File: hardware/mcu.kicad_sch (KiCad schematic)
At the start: 65 parts, among them J501 TC2050, J502 PRPC006SAAN-RC, J503 PRPC006SAAN-RC, J504 PRPC006SAAN-RC, J505 PRPC006SAAN-RC, J506 PRPC006SAAN-RC, J507 PRPC006SAAN-RC, J508 PRPC006SAAN-RC, J509 PRPC001DAAN-RC, Q501 BSS806NH, U501 STM32L552CEU6, U502 AT25SF081B-MAHB-T, Y501 ECS-160-9-37-CKM-TR3, Y502 ABS05-32.768KHZ-9-T

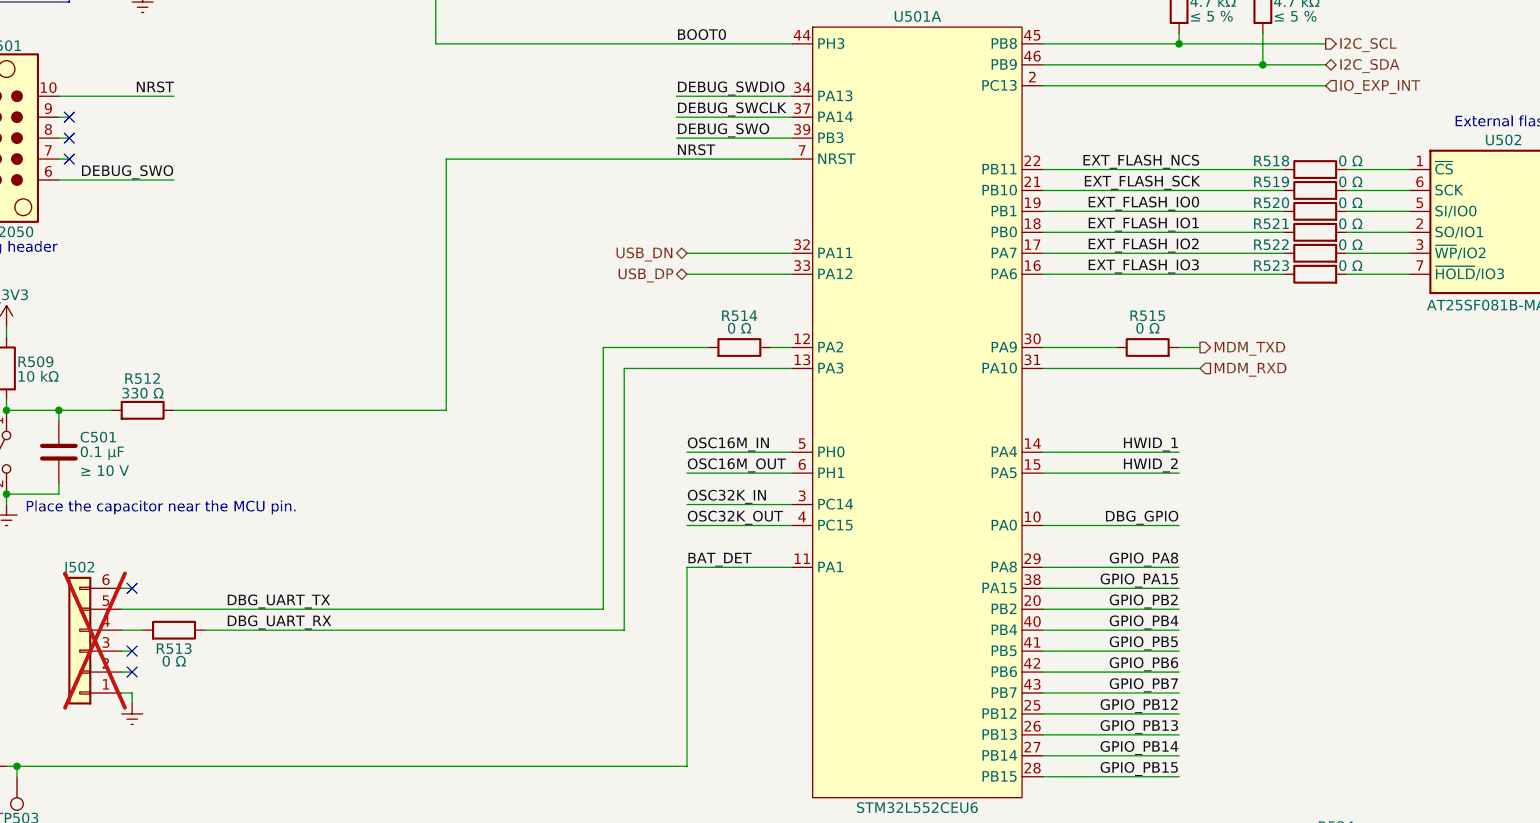
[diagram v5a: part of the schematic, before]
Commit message: HW: Set terminator resistors
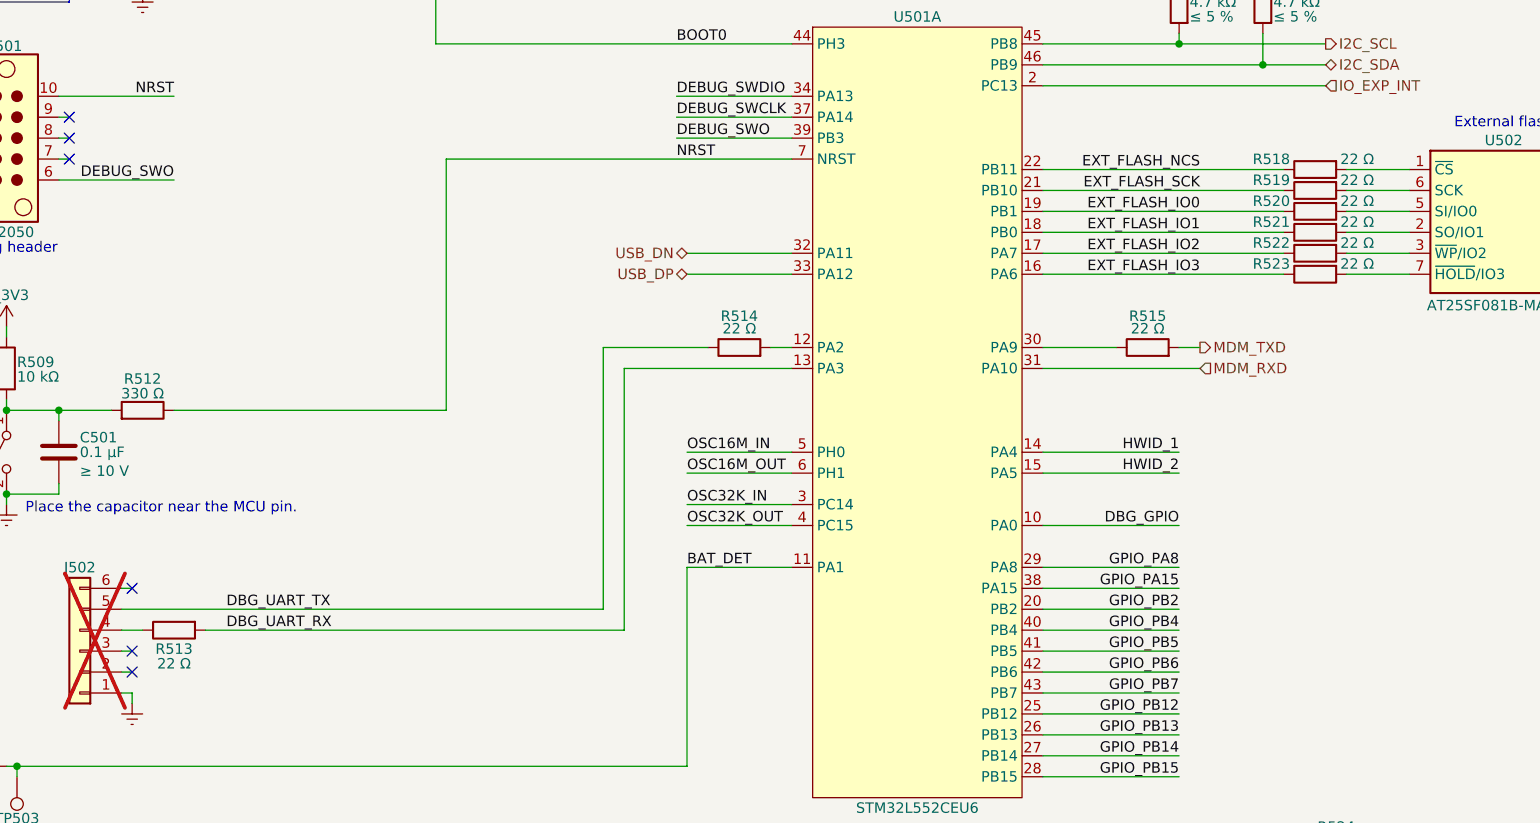
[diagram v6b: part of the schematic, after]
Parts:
- R513, R514, R515, R518, R519, R520, R521, R522, R523: value 0 Ω -> 22 Ω; DigiKey Part Number 732-560112110001CT-ND -> 732-560112110046CT-ND; MPN 560112110001 -> 560112110046
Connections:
- net DBG_UART_RX: now also R513.2; no longer R513.1
- net DBG_UART_TX: now also R514.1; no longer R514.2
- net at J502.4 (Pin_4): now also R513.1; no longer R513.2
- net at U501.12 (PA2): now also R514.2; no longer R514.1

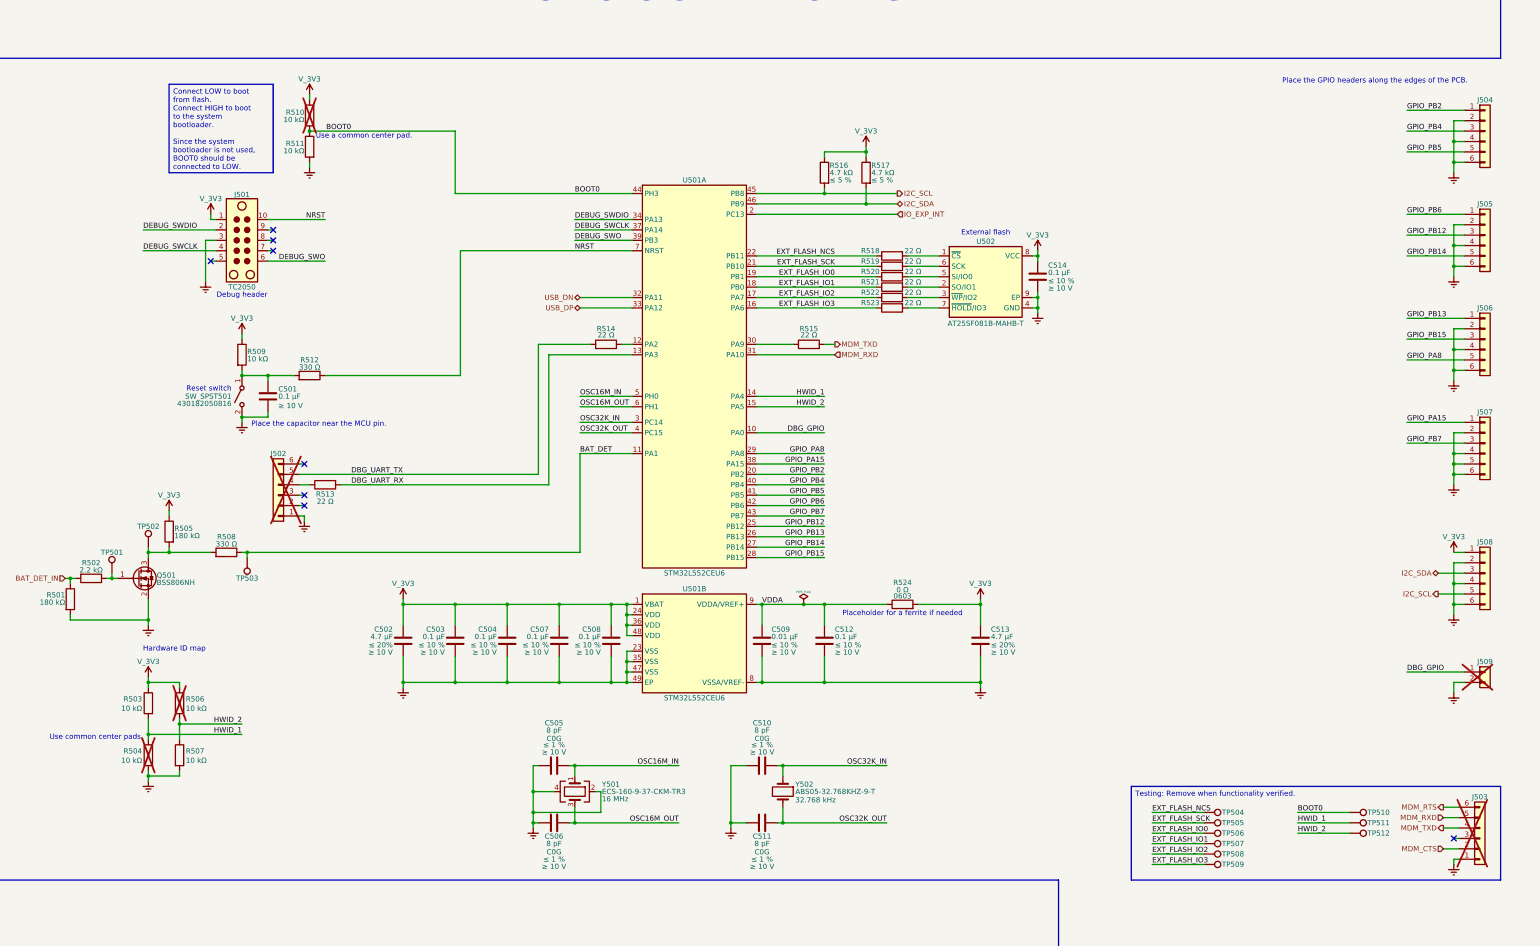
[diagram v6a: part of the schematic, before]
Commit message: HW: Refactor reference designators
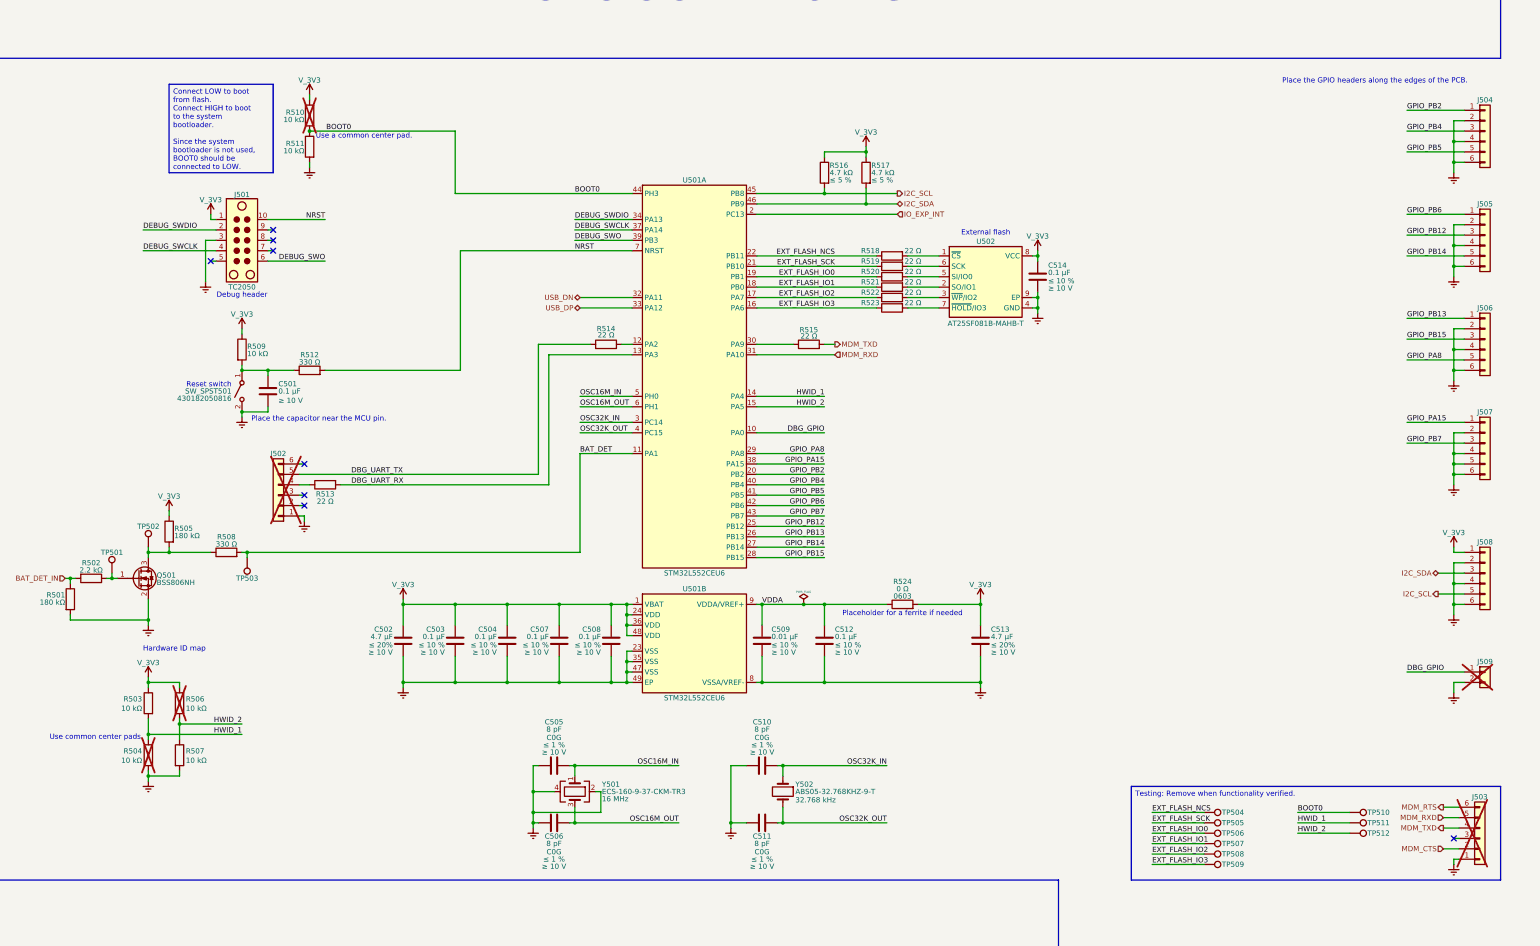
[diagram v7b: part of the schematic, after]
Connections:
- net BAT_DET: now also R508.2; no longer R508.1
- net NRST: now also R512.2; no longer R512.1
- net at C501.1, R509.2, SW_SPST501.1 (A): now also R512.1; no longer R512.2
- net at Q501.3 (D), R505.2, TP502.1: now also R508.1; no longer R508.2
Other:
- moved on the sheet: C501, R509, SW_SPST501
